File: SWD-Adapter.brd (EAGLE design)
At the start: 35.8 x 36.5 mm, 16 parts

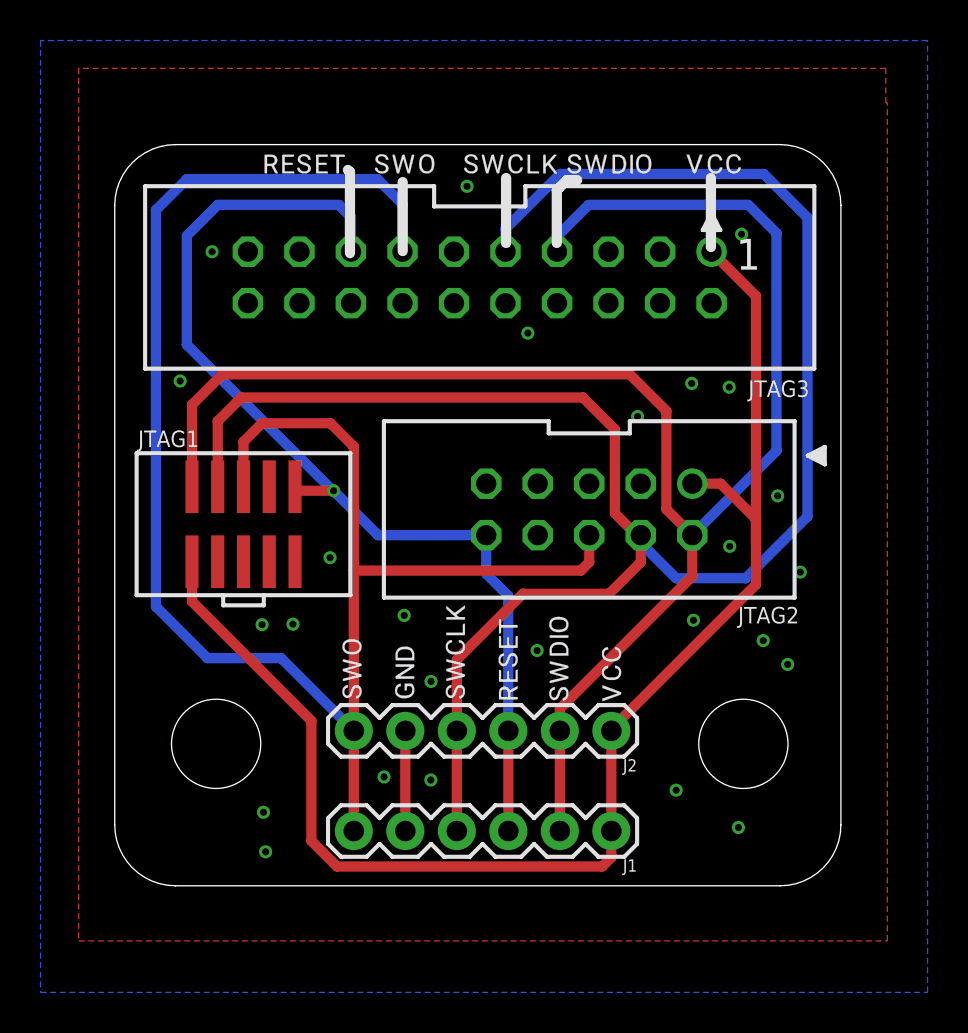
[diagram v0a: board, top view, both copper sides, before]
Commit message: add 6pin TC2030 pinout to SWD-Adapter variant
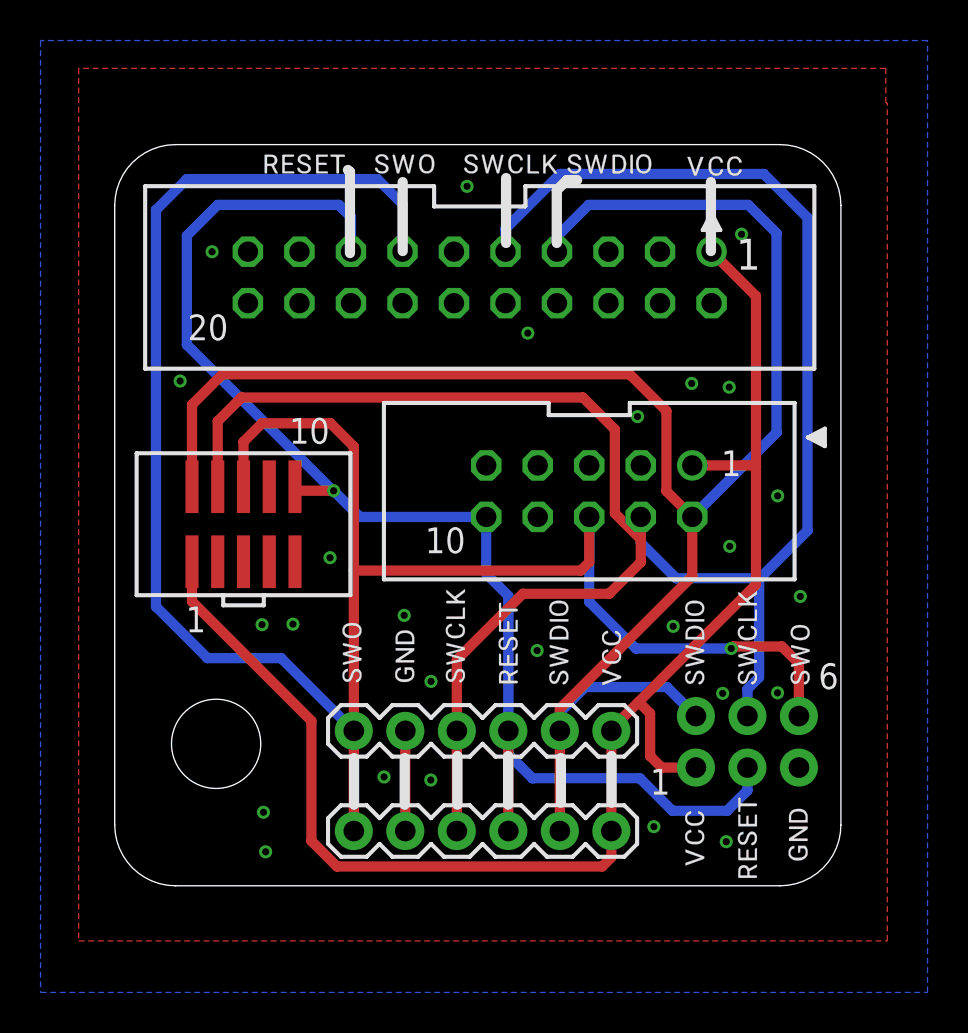
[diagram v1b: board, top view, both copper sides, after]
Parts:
- added J3: (no value), SparkFun-Connectors:2X3-NS
- added U$12: (no value), output:SWO0
- added U$13: (no value), output:RESET0
- added U$14: (no value), output:VCC0
- added U$15: (no value), output:GND0
- added U$16: (no value), output:SWCLK0
- added U$17: (no value), output:SWDIO0
- moved JTAG2 0.90 mm to (23.4, 38.5)
- moved U$1 0.80 mm to (11.7, 28.3)
- moved U$2 0.80 mm to (14.3, 28.3)
- moved U$3 0.80 mm to (16.8, 28.3)
- moved U$4 0.80 mm to (19.4, 28.2)
- moved U$5 0.80 mm to (21.9, 28.2)
- moved U$6 0.80 mm to (24.5, 28.2)
- moved U$10 0.12 mm to (27.5, 54.5)
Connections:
- net GND: now also J3.5
- net RESET: now also J3.3
- net SWCLK: now also J3.4
- net SWDIO: now also J3.2
- net SWO: now also J3.6
- net VCC: now also J3.1
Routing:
- net SWO: track 88.1 -> 107.4 mm, vias 0 -> 1
- net RESET: track 51.7 -> 67.9 mm
- net SWCLK: track 94.1 -> 103.3 mm
- net SWDIO: track 82.2 -> 90.0 mm
- net VCC: track 70.4 -> 74.0 mm
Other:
- board text added: "1"
- board text added: "10"
- board text added: "20"
- board text added: "6"
